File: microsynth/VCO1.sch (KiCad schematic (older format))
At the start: 24 parts, among them SW22 SW_SPST, U11 LM741, U12 LM741, U13 LM741, U14 4016, U5 LF347

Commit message: Proper capacitor footprints
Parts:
- C15, C17: footprint Capacitor_THT:C_Disc_D5.0mm_W2.5mm_P5.00mm -> Capacitor_THT:C_Rect_L7.2mm_W2.5mm_P5.00mm_FKS2_FKP2_MKS2_MKP2
- C16: footprint Capacitor_THT:C_Disc_D5.0mm_W2.5mm_P5.00mm -> Capacitor_THT:C_Rect_L7.2mm_W3.5mm_P5.00mm_FKS2_FKP2_MKS2_MKP2
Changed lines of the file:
@@
 F 0 "C16" V 1598 3150 50  0000 C CNN
 F 1 "15n" V 1689 3150 50  0000 C CNN
-F 2 "Capacitor_THT:C_Disc_D5.0mm_W2.5mm_P5.00mm" H 1888 3000 50  0001 C CNN
+F 2 "Capacitor_THT:C_Rect_L7.2mm_W3.5mm_P5.00mm_FKS2_FKP2_MKS2_MKP2" H 1888 3000 50  0001 C CNN
 F 3 "~" H 1850 3150 50  0001 C CNN
 	1    1850 3150
@@
 F 0 "C17" V 2698 3900 50  0000 C CNN
 F 1 "10n" V 2789 3900 50  0000 C CNN
-F 2 "Capacitor_THT:C_Disc_D5.0mm_W2.5mm_P5.00mm" H 2988 3750 50  0001 C CNN
+F 2 "Capacitor_THT:C_Rect_L7.2mm_W2.5mm_P5.00mm_FKS2_FKP2_MKS2_MKP2" H 2988 3750 50  0001 C CNN
 F 3 "~" H 2950 3900 50  0001 C CNN
 	1    2950 3900
@@
 F 0 "C15" V 2298 1400 50  0000 C CNN
 F 1 "10n" V 2389 1400 50  0000 C CNN
-F 2 "Capacitor_THT:C_Disc_D5.0mm_W2.5mm_P5.00mm" H 2588 1250 50  0001 C CNN
+F 2 "Capacitor_THT:C_Rect_L7.2mm_W2.5mm_P5.00mm_FKS2_FKP2_MKS2_MKP2" H 2588 1250 50  0001 C CNN
 F 3 "~" H 2550 1400 50  0001 C CNN
 	1    2550 1400

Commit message: Clean up repo
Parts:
- U5: symbol Amplifier_Operational:LF347 -> microsynth-rescue:LF347-Amplifier_Operational
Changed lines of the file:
@@
 	2450 950  2450 1500
 $Comp
-L Amplifier_Operational:LF347 U?
+L microsynth-rescue:LF347-Amplifier_Operational U?
 U 4 1 5E920B31
 P 3150 1900
 AR Path="/5E8C1704/5E920B31" Ref="U?"  Part="4"
 AR Path="/5E222DC1/5E920B31" Ref="U5"  Part="4"
+AR Path="/5E920B31" Ref="U5"  Part="4"
 F 0 "U5" H 3150 1500 50  0000 C CNN
 F 1 "LF347" H 3150 1600 50  0000 C CNN

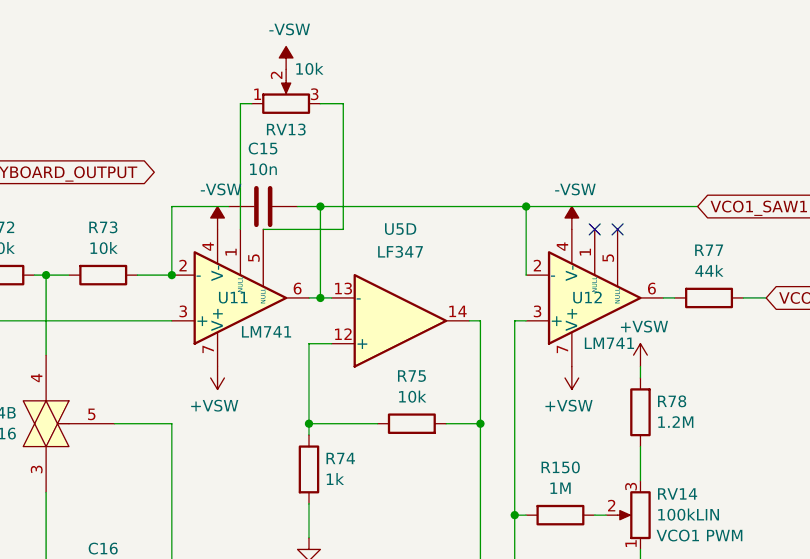
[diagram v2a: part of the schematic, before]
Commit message: Replace dodgy parts 1458, 4136 & LF351s
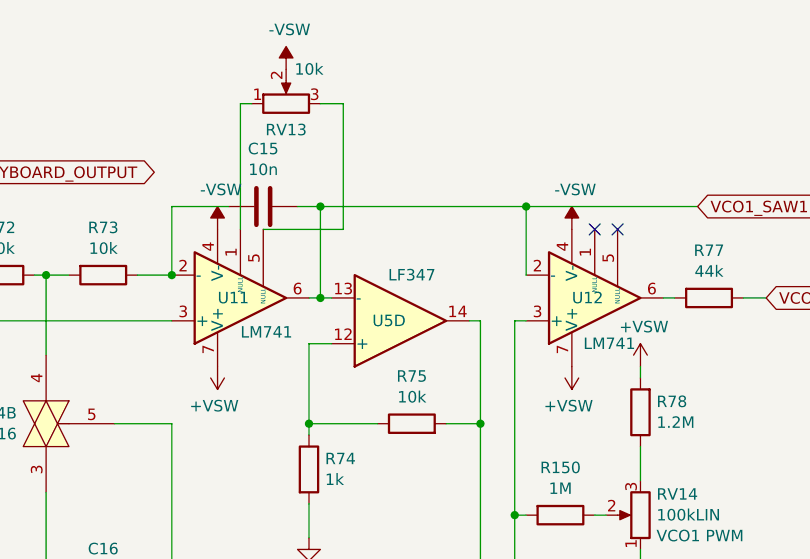
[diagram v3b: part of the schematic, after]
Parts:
- removed U5: LF347, Package_DIP:DIP-14_W7.62mm_LongPads, symbol microsynth-rescue:LF347-Amplifier_Operational
- added U5: LF347, Package_DIP:DIP-14_W7.62mm_LongPads, symbol pe_microsynth:LF347
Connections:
- net IC22_PIN_3: now also U5.14
- net VCO1_SAW1: now also U5.13 (-)
- net at R74.1, R75.1: now also U5.12 (+)
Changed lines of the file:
@@
 Wire Wire Line
 	2450 950  2450 1500
-$Comp
-L microsynth-rescue:LF347-Amplifier_Operational U?
-U 4 1 5E920B31
-P 3150 1900
-AR Path="/5E8C1704/5E920B31" Ref="U?"  Part="4"
-AR Path="/5E222DC1/5E920B31" Ref="U5"  Part="4"
-AR Path="/5E920B31" Ref="U5"  Part="4"
-F 0 "U5" H 3150 1500 50  0000 C CNN
-F 1 "LF347" H 3150 1600 50  0000 C CNN
-F 2 "Package_DIP:DIP-14_W7.62mm_LongPads" H 3100 2000 50  0001 C CNN
-F 3 "https://www.ti.com/lit/ds/symlink/lf147.pdf" H 3200 2100 50  0001 C CNN
-	4    3150 1900
-	1    0    0    1
-$EndComp
 Wire Wire Line
 	2450 4150 2450 4350
@@
 	-1   0    0    -1
 $EndComp
+$Comp
+L pe_microsynth:LF347 U?
+U 4 1 5EBFEEA3
+P 3150 1900
+AR Path="/5E8C1704/5EBFEEA3" Ref="U?"  Part="4"
+AR Path="/5E222DC1/5EBFEEA3" Ref="U5"  Part="4"
+F 0 "U5" H 3100 1900 50  0000 C CNN
+F 1 "LF347" H 3200 1700 50  0000 C CNN
+F 2 "Package_DIP:DIP-14_W7.62mm_LongPads" H 3100 2000 50  0001 C CNN
+F 3 "https://www.bitsbox.co.uk/data/analog/LF347.pdf" H 3200 2100 50  0001 C CNN
+	4    3150 1900
+	1    0    0    1
+$EndComp
 $EndSCHEMATC

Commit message: Consolidate all(?) switches
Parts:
- RV14: footprint 4ms_Potentiometer:Pot_16mm_NoDet_RV16AF-4A -> microsynth:Pot_16mm_NoDet_RV16AF-4A
- SW22: footprint 4ms:SPDT_KIT -> microsynth:SPDT_KIT
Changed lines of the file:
@@
 F 0 "RV14" H 4130 2659 50  0000 R CNN
 F 1 "100kLIN" H 4130 2750 50  0000 R CNN
-F 2 "4ms_Potentiometer:Pot_16mm_NoDet_RV16AF-4A" H 4200 2750 50  0001 C CNN
+F 2 "microsynth:Pot_16mm_NoDet_RV16AF-4A" H 4200 2750 50  0001 C CNN
 F 3 "~" H 4200 2750 50  0001 C CNN
 F 4 "VCO1 PWM" H 4130 2841 50  0000 R CNN "Label"
@@
 F 0 "SW22" V 1141 1162 50  0000 R CNN
 F 1 "SW_SPST" V 1050 1162 50  0000 R CNN
-F 2 "4ms:SPDT_KIT" H 1050 1250 50  0001 C CNN
+F 2 "microsynth:SPDT_KIT" H 1050 1250 50  0001 C CNN
 F 3 "~" H 1050 1250 50  0001 C CNN
 F 4 "VCO1 On/Off" V 959 1162 50  0000 R CNN "Label"

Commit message: Annotate schematic
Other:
- note added: "VCO1 ON/OFF"
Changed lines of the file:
@@
 	1    0    0    1
 $EndComp
+Text Notes 900  1050 0    50   ~ 0
+VCO1 ON/OFF
 $EndSCHEMATC
